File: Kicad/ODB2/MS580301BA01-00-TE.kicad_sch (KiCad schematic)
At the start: 0 parts

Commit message: edit titles
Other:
- company: (none) -> GAUL
- title: (none) -> Barometer
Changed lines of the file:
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@@
 	(generator_version "8.0")
 	(paper "A4")
+	(title_block
+		(title "Barometer")
+		(date "2024-11-09")
+		(company "GAUL")
+	)
 )

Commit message: add titles
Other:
- note added: "Barometer"
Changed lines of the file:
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@@
 		(company "GAUL")
 	)
+	(text "Barometer"
+		(exclude_from_sim no)
+		(at 36.068 18.034 0)
+		(effects
+			(font
+				(size 6 6)
+				(thickness 1.2)
+				(bold yes)
+			)
+		)
+	)
 )

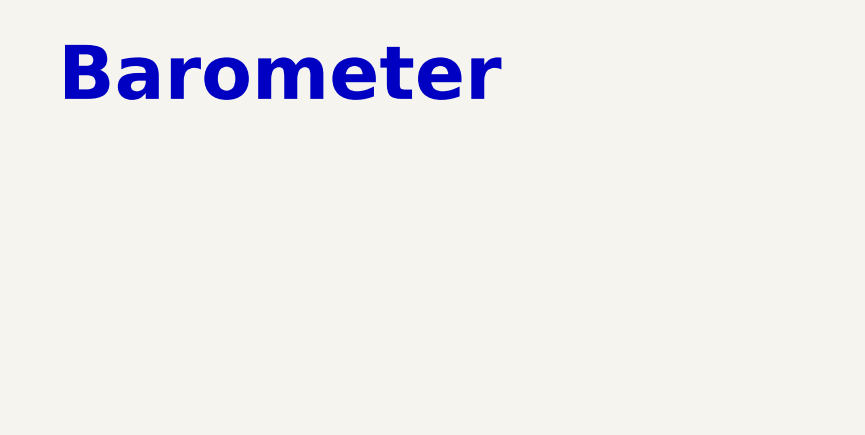
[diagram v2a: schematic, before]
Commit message: add sensors
ICM
L76L
MS580
PowerSupply
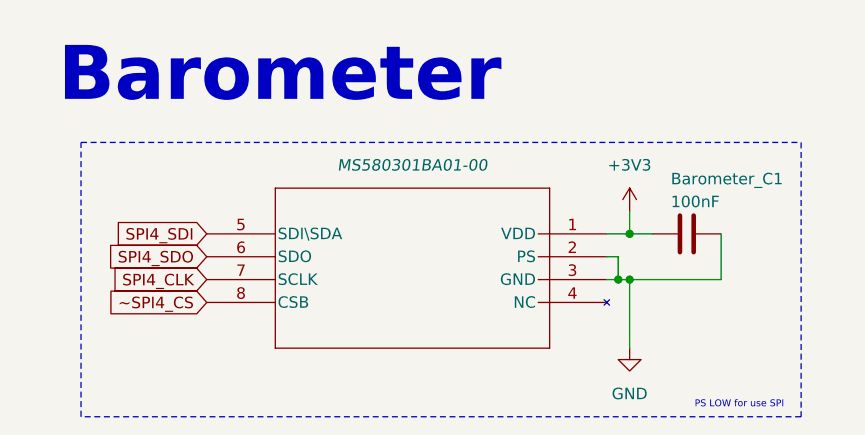
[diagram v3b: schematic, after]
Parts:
- added Barometer_C1: 100nF, symbol Device:C
- added U7: MS580301BA01-00, MS5803-01BA01_TEC, symbol ODB_Lib:MS580301BA01-00
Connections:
- new net +3V3: Barometer_C1.2, U7.1 (VDD)
- new net GND: Barometer_C1.1, U7.2 (PS), U7.3 (GND)
- new net SPI4_CLK: U7.7 (SCLK)
- new net SPI4_SDI: U7.5 (SDI\SDA)
- new net SPI4_SDO: U7.6 (SDO)
- new net ~SPI4_CS: U7.8 (CSB)
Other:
- note added: "PS LOW for use SPI"

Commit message: fix spi icm pinout
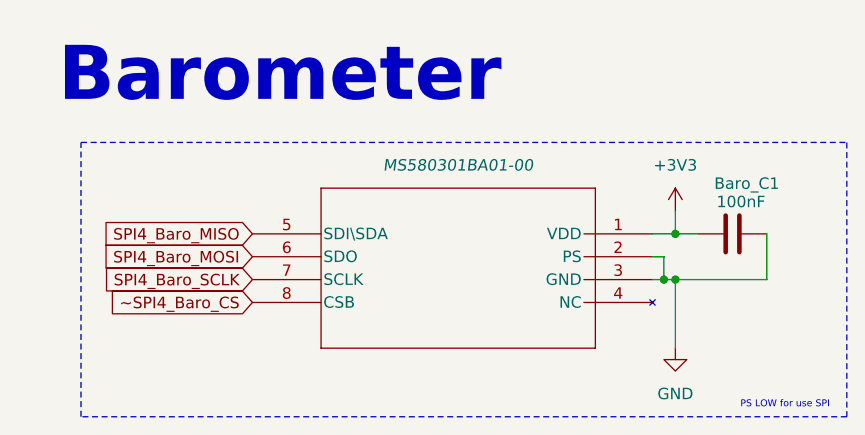
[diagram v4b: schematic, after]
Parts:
- renumbered Barometer_C1 to Baro_C1
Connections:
- net SPI4_CLK renamed SPI4_Baro_SCLK
- net SPI4_SDI renamed SPI4_Baro_MISO
- net SPI4_SDO renamed SPI4_Baro_MOSI
- net ~SPI4_CS renamed ~SPI4_Baro_CS
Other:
- moved on the sheet: Baro_C1
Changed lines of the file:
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@@
 	)
 	(junction
-		(at 74.93 40.64)
+		(at 80.01 40.64)
 		(diameter 0)
 		(color 0 0 0 0)
 	)
 	(junction
-		(at 73.66 40.64)
+		(at 78.74 40.64)
 		(diameter 0)
 		(color 0 0 0 0)
 	)
 	(junction
-		(at 74.93 35.56)
+		(at 80.01 35.56)
 		(diameter 0)
 		(color 0 0 0 0)
@@
 	(wire
 		(pts
-			(xy 72.39 40.64) (xy 73.66 40.64)
-		)
-		(stroke
-			(width 0)
-			(type default)
-		)
-	)
-	(wire
-		(pts
-			(xy 73.66 40.64) (xy 74.93 40.64)
-		)
-		(stroke
-			(width 0)
-			(type default)
-		)
-	)
-	(wire
-		(pts
-			(xy 85.09 40.64) (xy 74.93 40.64)
-		)
-		(stroke
-			(width 0)
-			(type default)
-		)
-	)
-	(wire
-		(pts
-			(xy 72.39 35.56) (xy 74.93 35.56)
-		)
-		(stroke
-			(width 0)
-			(type default)
-		)
-	)
-	(wire
-		(pts
-			(xy 73.66 38.1) (xy 73.66 40.64)
-		)
-		(stroke
-			(width 0)
-			(type default)
-		)
-	)
-	(wire
-		(pts
-			(xy 74.93 40.64) (xy 74.93 48.26)
-		)
-		(stroke
-			(width 0)
-			(type default)
-		)
-	)
-	(wire
-		(pts
-			(xy 74.93 33.02) (xy 74.93 35.56)
-		)
-		(stroke
-			(width 0)
-			(type default)
-		)
-	)
-	(wire
-		(pts
-			(xy 72.39 38.1) (xy 73.66 38.1)
-		)
-		(stroke
-			(width 0)
-			(type default)
-		)
-	)
-	(wire
-		(pts
-			(xy 85.09 35.56) (xy 85.09 40.64)
-		)
-		(stroke
-			(width 0)
-			(type default)
-		)
-	)
-	(wire
-		(pts
-			(xy 74.93 35.56) (xy 77.47 35.56)
+			(xy 77.47 40.64) (xy 78.74 40.64)
+		)
+		(stroke
+			(width 0)
+			(type default)
+		)
+	)
+	(wire
+		(pts
+			(xy 78.74 40.64) (xy 80.01 40.64)
+		)
+		(stroke
+			(width 0)
+			(type default)
+		)
+	)
+	(wire
+		(pts
+			(xy 90.17 40.64) (xy 80.01 40.64)
+		)
+		(stroke
+			(width 0)
+			(type default)
+		)
+	)
+	(wire
+		(pts
+			(xy 77.47 35.56) (xy 80.01 35.56)
+		)
+		(stroke
+			(width 0)
+			(type default)
+		)
+	)
+	(wire
+		(pts
+			(xy 78.74 38.1) (xy 78.74 40.64)
+		)
+		(stroke
+			(width 0)
+			(type default)
+		)
+	)
+	(wire
+		(pts
+			(xy 80.01 40.64) (xy 80.01 48.26)
+		)
+		(stroke
+			(width 0)
+			(type default)
+		)
+	)
+	(wire
+		(pts
+			(xy 80.01 33.02) (xy 80.01 35.56)
+		)
+		(stroke
+			(width 0)
+			(type default)
+		)
+	)
+	(wire
+		(pts
+			(xy 77.47 38.1) (xy 78.74 38.1)
+		)
+		(stroke
+			(width 0)
+			(type default)
+		)
+	)
+	(wire
+		(pts
+			(xy 90.17 35.56) (xy 90.17 40.64)
+		)
+		(stroke
+			(width 0)
+			(type default)
+		)
+	)
+	(wire
+		(pts
+			(xy 80.01 35.56) (xy 82.55 35.56)
 		)
 		(stroke
@@
 	(rectangle
 		(start 13.97 25.4)
-		(end 93.98 55.88)
+		(end 99.06 55.88)
 		(stroke
 			(width 0)
@@
 	(text "PS LOW for use SPI"
 		(exclude_from_sim no)
-		(at 87.122 54.61 0)
+		(at 92.202 54.61 0)
 		(effects
 			(font
@@
 		)
 	)
-	(global_label "SPI4_CLK"
+	(global_label "SPI4_Baro_SCLK"
 		(shape input)
-		(at 27.94 40.64 180)
+		(at 33.02 40.64 180)
 		(fields_autoplaced yes)
 		(effects
@@
 		)
 		(property "Intersheetrefs" "${INTERSHEET_REFS}"
-			(at 16.1253 40.64 0)
+			(at 14.674 40.64 0)
 			(effects
 				(font
@@
 		)
 	)
-	(global_label "SPI4_SDO"
+	(global_label "SPI4_Baro_MOSI"
 		(shape input)
-		(at 27.94 38.1 180)
+		(at 33.02 38.1 180)
 		(fields_autoplaced yes)
 		(effects
@@
 		)
 		(property "Intersheetrefs" "${INTERSHEET_REFS}"
-			(at 15.8834 38.1 0)
+			(at 14.8554 38.1 0)
 			(effects
 				(font
@@
 		)
 	)
-	(global_label "~SPI4_CS"
+	(global_label "~SPI4_Baro_CS"
 		(shape input)
-		(at 27.94 43.18 180)
+		(at 33.02 43.18 180)
 		(fields_autoplaced yes)
 		(effects
@@
 		)
 		(property "Intersheetrefs" "${INTERSHEET_REFS}"
-			(at 16.3068 43.18 0)
+			(at 16.065 43.18 0)
 			(effects
 				(font
@@
 		)
 	)
-	(global_label "SPI4_SDI"
+	(global_label "SPI4_Baro_MISO"
 		(shape input)
-		(at 27.94 35.56 180)
+		(at 33.02 35.56 180)
 		(fields_autoplaced yes)
 		(effects
@@
 		)
 		(property "Intersheetrefs" "${INTERSHEET_REFS}"
-			(at 16.6091 35.56 0)
+			(at 14.8554 35.56 0)
 			(effects
 				(font
@@
 	(symbol
 		(lib_id "power:+3V3")
-		(at 74.93 33.02 0)
+		(at 80.01 33.02 0)
 		(unit 1)
 		(exclude_from_sim no)
@@
 		(fields_autoplaced yes)
 		(property "Reference" "#PWR057"
-			(at 74.93 36.83 0)
+			(at 80.01 36.83 0)
 			(effects
 				(font
@@
 		)
 		(property "Value" "+3V3"
-			(at 74.93 27.94 0)
+			(at 80.01 27.94 0)
 			(effects
 				(font
@@
 		)
 		(property "Footprint" ""
-			(at 74.93 33.02 0)
+			(at 80.01 33.02 0)
 			(effects
 				(font
@@
 		)
 		(property "Datasheet" ""
-			(at 74.93 33.02 0)
+			(at 80.01 33.02 0)
 			(effects
 				(font
@@
 		)
 		(property "Description" "Power symbol creates a global label with name \"+3V3\""
-			(at 74.93 33.02 0)
+			(at 80.01 33.02 0)
 			(effects
 				(font
@@
 	(symbol
 		(lib_id "power:GND")
-		(at 74.93 48.26 0)
+		(at 80.01 48.26 0)
 		(unit 1)
 		(exclude_from_sim no)
@@
 		(fields_autoplaced yes)
 		(property "Reference" "#PWR058"
-			(at 74.93 54.61 0)
+			(at 80.01 54.61 0)
 			(effects
 				(font
@@
 		)
 		(property "Value" "GND"
-			(at 74.93 53.34 0)
+			(at 80.01 53.34 0)
 			(effects
 				(font
@@
 		)
 		(property "Footprint" ""
-			(at 74.93 48.26 0)
+			(at 80.01 48.26 0)
 			(effects
 				(font
@@
 		)
 		(property "Datasheet" ""
-			(at 74.93 48.26 0)
+			(at 80.01 48.26 0)
 			(effects
 				(font
@@
 		)
 		(property "Description" "Power symbol creates a global label with name \"GND\" , ground"
-			(at 74.93 48.26 0)
+			(at 80.01 48.26 0)
 			(effects
 				(font
@@
 	(symbol
 		(lib_id "ODB_Lib:MS580301BA01-00")
-		(at 27.94 35.56 0)
+		(at 33.02 35.56 0)
 		(unit 1)
 		(exclude_from_sim no)
@@
 		(fields_autoplaced yes)
 		(property "Reference" "U7"
-			(at 50.8 25.4 0)
+			(at 55.88 25.4 0)
 			(effects
 				(font
@@
 		)
 		(property "Value" "MS580301BA01-00"
-			(at 50.8 27.94 0)
+			(at 55.88 27.94 0)
 			(effects
 				(font
@@
 		)
 		(property "Footprint" "MS5803-01BA01_TEC"
-			(at 51.054 23.114 0)
+			(at 56.134 23.114 0)
 			(effects
 				(font
@@
 		)
 		(property "Datasheet" "MS580301BA01-00"
-			(at 50.8 27.94 0)
+			(at 55.88 27.94 0)
 			(effects
 				(font
@@
 		)
 		(property "Description" ""
-			(at 27.94 35.56 0)
+			(at 33.02 35.56 0)
 			(effects
 				(font
@@
 	(symbol
 		(lib_id "Device:C")
-		(at 81.28 35.56 270)
+		(at 86.36 35.56 270)
 		(mirror x)
 		(unit 1)
@@
 		(on_board yes)
 		(dnp no)
-		(property "Reference" "Barometer_C1"
-			(at 79.502 29.464 90)
+		(property "Reference" "Baro_C1"
+			(at 84.328 29.972 90)
 			(effects
 				(font
@@
 		)
 		(property "Value" "100nF"
-			(at 79.502 32.004 90)
+			(at 84.582 32.004 90)
 			(effects
 				(font
@@
 		)
 		(property "Footprint" ""
-			(at 77.47 34.5948 0)
+			(at 82.55 34.5948 0)
 			(effects
 				(font
@@
 		)
 		(property "Datasheet" "~"
-			(at 81.28 35.56 0)
+			(at 86.36 35.56 0)
 			(effects
 				(font
@@
 		)
 		(property "Description" "Unpolarized capacitor"
-			(at 81.28 35.56 0)
+			(at 86.36 35.56 0)
 			(effects
 				(font
@@
 			(project "ODB2"
 				(path "/4b06c5d1-aa8b-48ed-8972-b43a60cfab78/eac5f07f-d6a3-4c95-b286-7cebf46e30db/a22c617e-0d66-4985-a85f-0ed5b022cb45"
-					(reference "Barometer_C1")
+					(reference "Baro_C1")
 					(unit 1)
 				)

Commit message: fix label
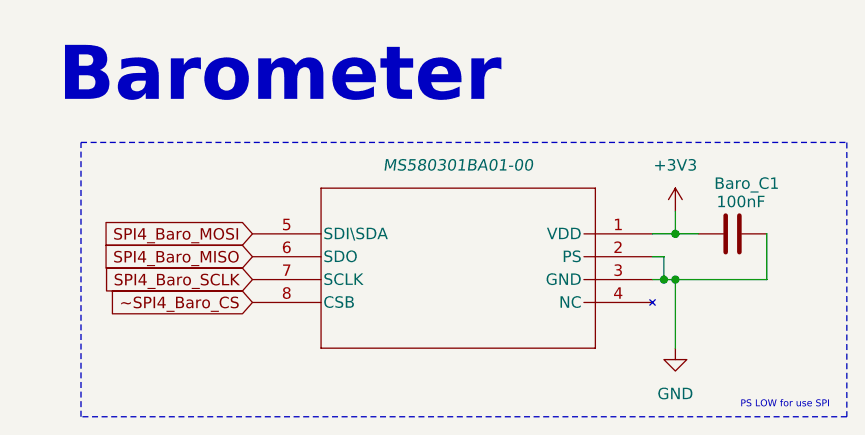
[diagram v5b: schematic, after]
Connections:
- net SPI4_Baro_MISO: now also U7.6 (SDO); no longer U7.5 (SDI\SDA)
- net SPI4_Baro_MOSI: now also U7.5 (SDI\SDA); no longer U7.6 (SDO)
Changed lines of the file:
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@@
 		)
 	)
-	(global_label "SPI4_Baro_MOSI"
+	(global_label "SPI4_Baro_MISO"
 		(shape input)
 		(at 33.02 38.1 180)
@@
 		)
 	)
-	(global_label "SPI4_Baro_MISO"
+	(global_label "SPI4_Baro_MOSI"
 		(shape input)
 		(at 33.02 35.56 180)

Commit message: Revert "fix pinout"
This reverts commit f7fb1bb1343b18ec7defcf1dc44a3e70818eed55.
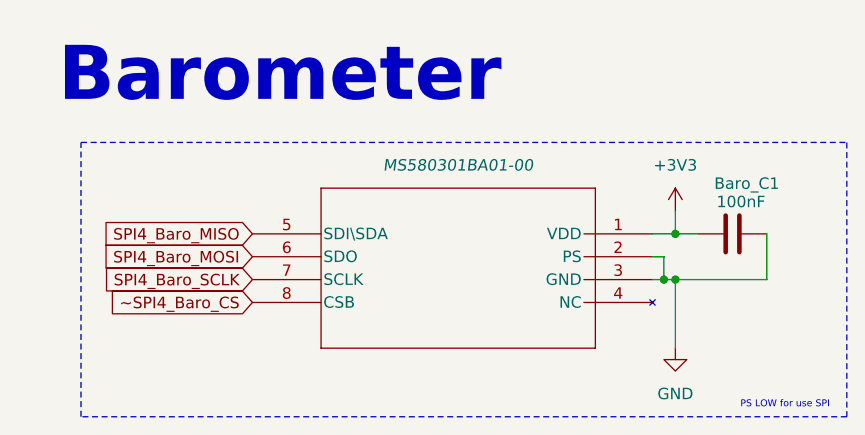
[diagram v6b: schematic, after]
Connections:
- net SPI4_Baro_MISO: now also U7.5 (SDI\SDA); no longer U7.6 (SDO)
- net SPI4_Baro_MOSI: now also U7.6 (SDO); no longer U7.5 (SDI\SDA)
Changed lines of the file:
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@@
 		)
 	)
-	(global_label "SPI4_Baro_MISO"
+	(global_label "SPI4_Baro_MOSI"
 		(shape input)
 		(at 33.02 38.1 180)
@@
 		)
 	)
-	(global_label "SPI4_Baro_MOSI"
+	(global_label "SPI4_Baro_MISO"
 		(shape input)
 		(at 33.02 35.56 180)
